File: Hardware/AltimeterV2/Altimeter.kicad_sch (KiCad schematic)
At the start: 18 parts, among them J1 Conn_01x06, U1 MS580301BA01-00, U2 MS580301BA01-00, U3 NUP4202

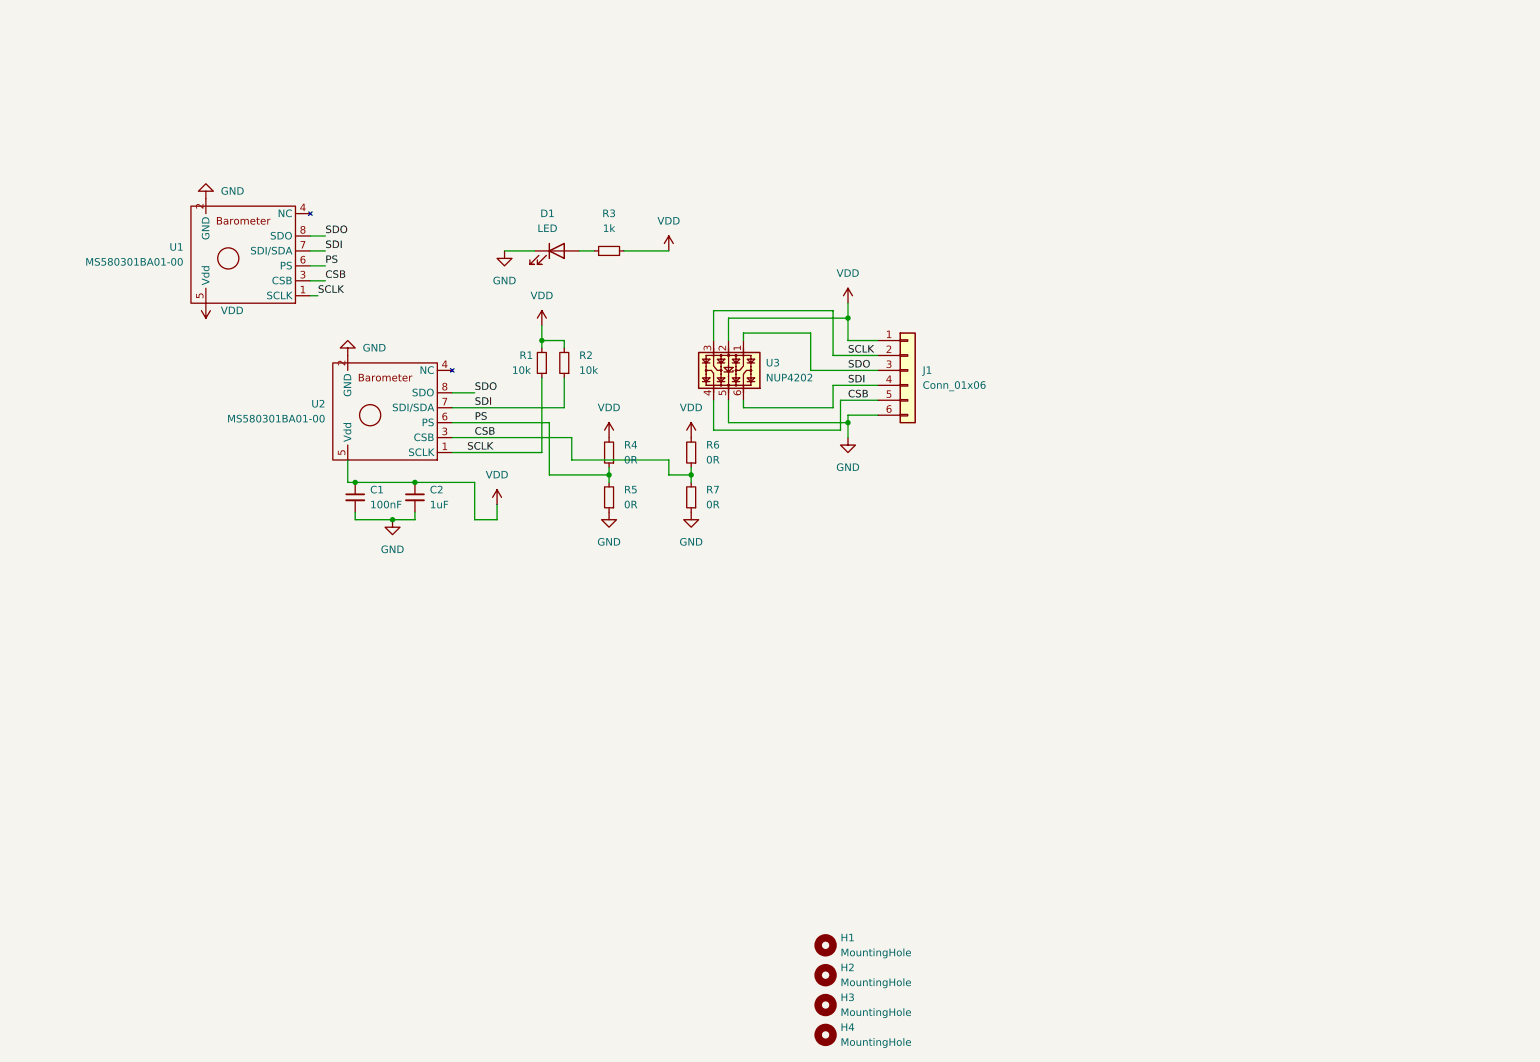
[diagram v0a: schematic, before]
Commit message: update to altimeter pcb
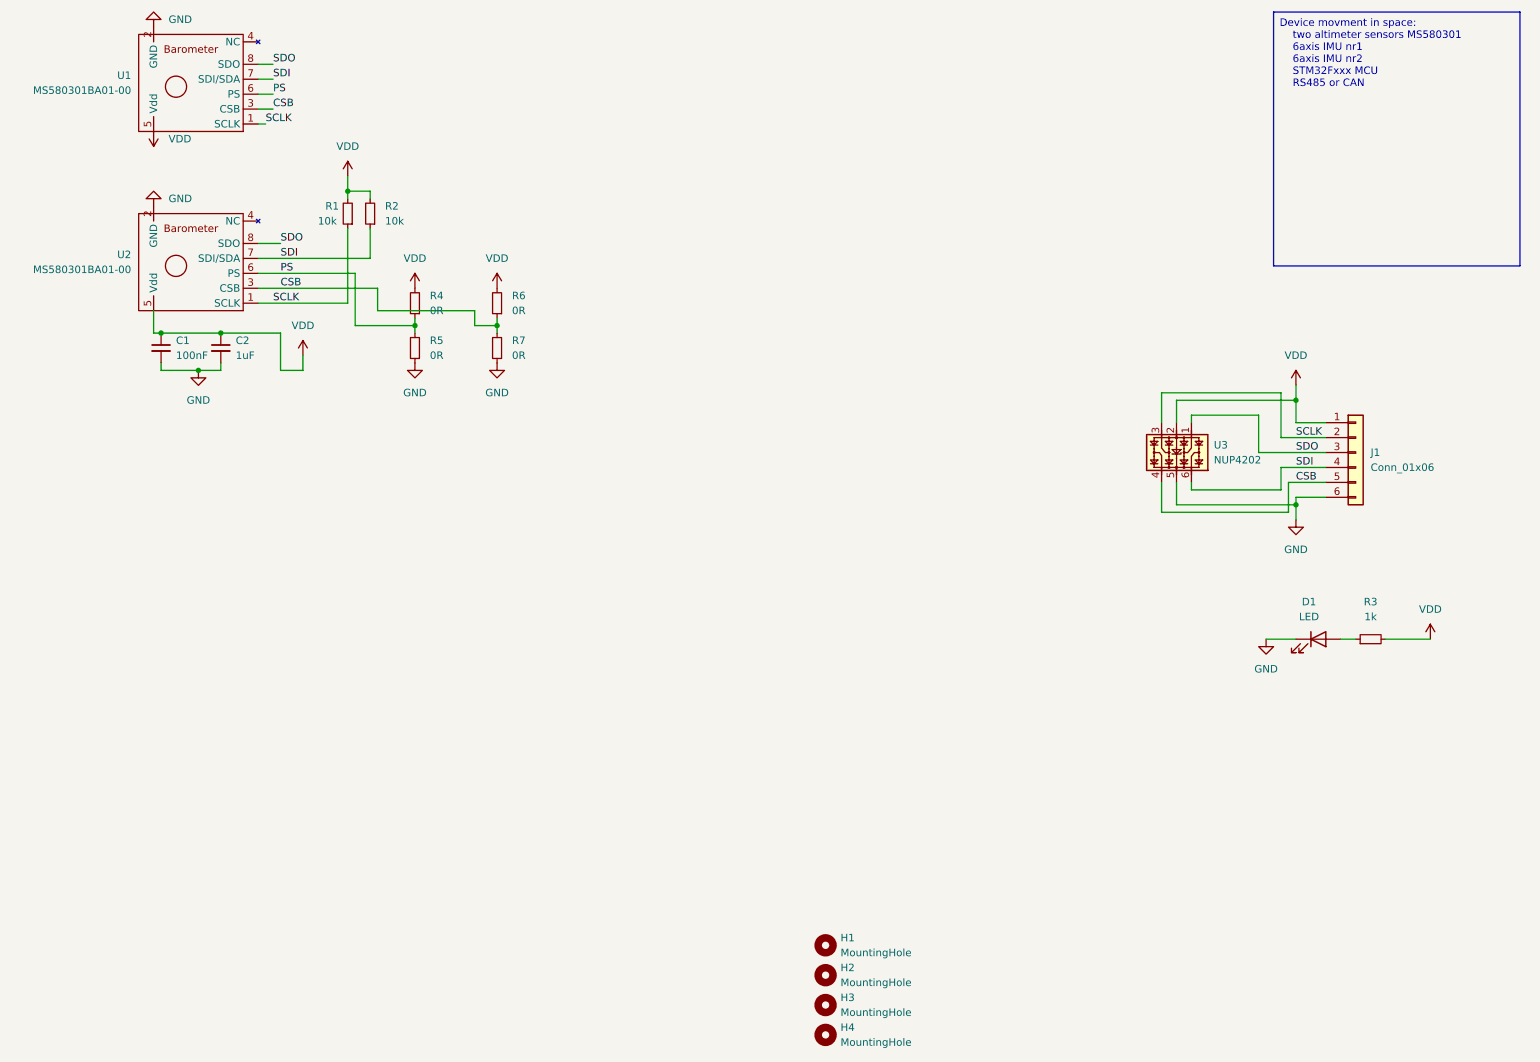
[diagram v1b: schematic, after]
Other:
- moved on the sheet: C1, C2, D1, J1, R1, R2, R3, R4, R5, R6, R7, U1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
